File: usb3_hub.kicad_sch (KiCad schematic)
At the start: 63 parts, among them Q2601 QS6M4, U2601 UPD720210K8-BAF-A, Y2601 24MHz

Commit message: Fix schematic ERC errors
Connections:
- net U34.D+: no longer names the net of U2601.35 (U2DP4)
- net U34.D-: no longer names the net of U2601.36 (U2DN4)
- net U34.RX+: no longer names the net of U2601.32 (U3RXDP4)
- net U34.RX-: no longer names the net of U2601.33 (U3RXDN4)
- net U34.TX+: no longer names the net of U2601.29 (U3TXDP4)
- net U34.TX-: no longer names the net of U2601.30 (U3TXDN4)
- no-connect marks 2 -> 8

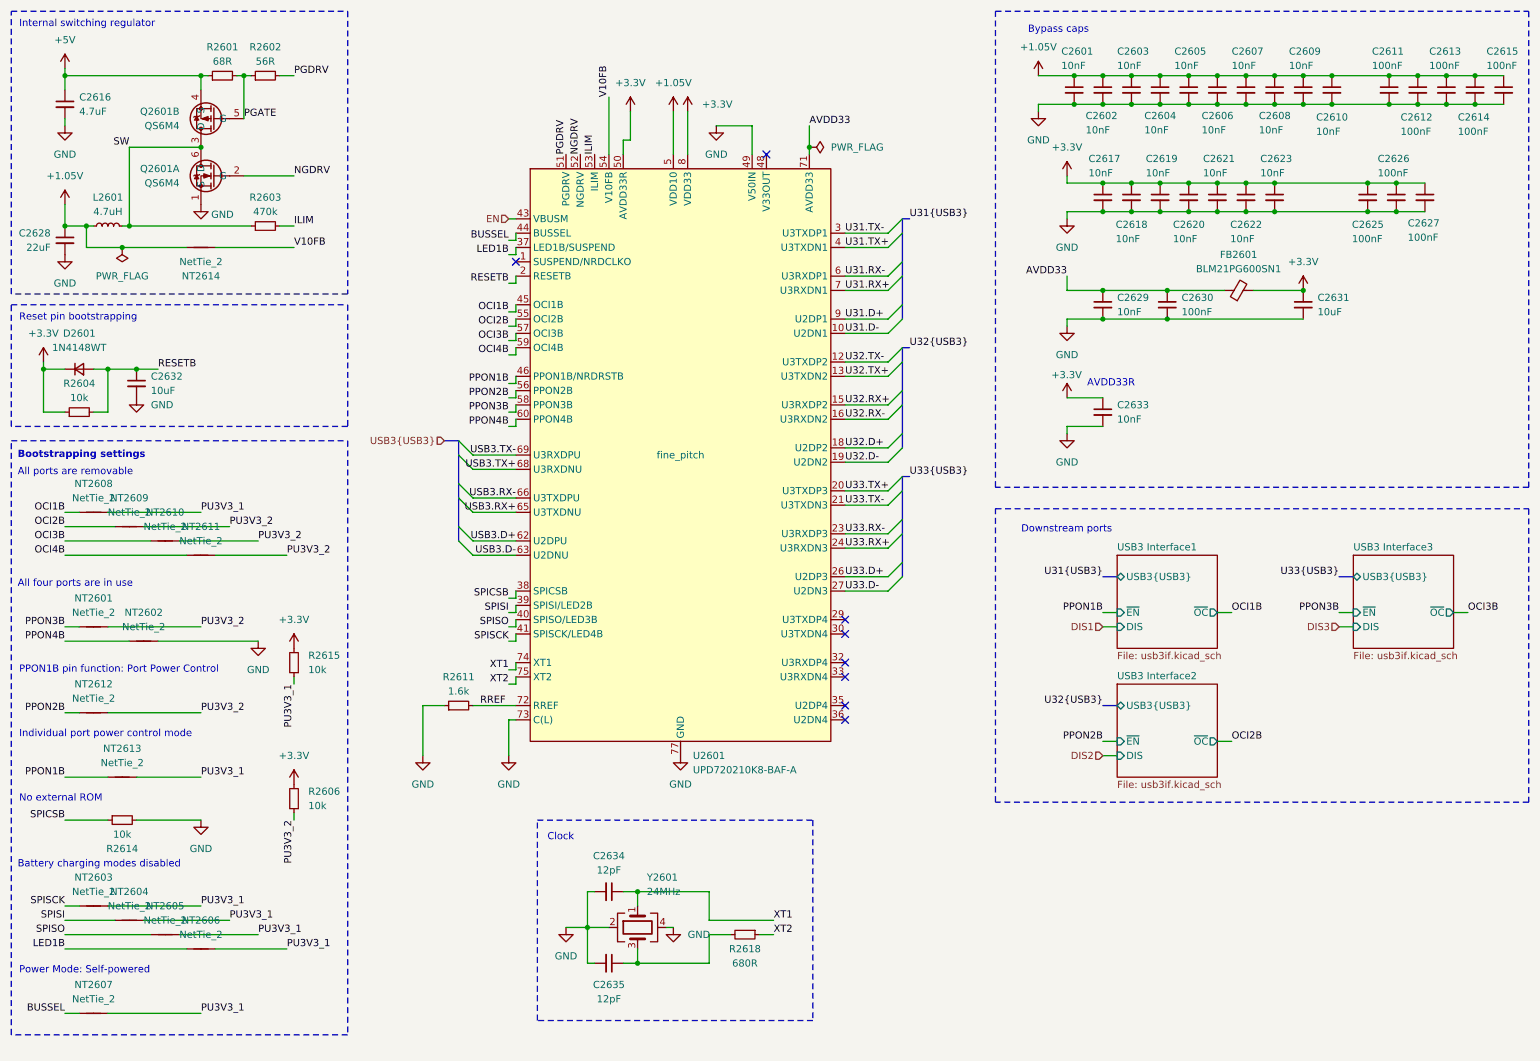
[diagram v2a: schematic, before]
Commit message: Reannotate components
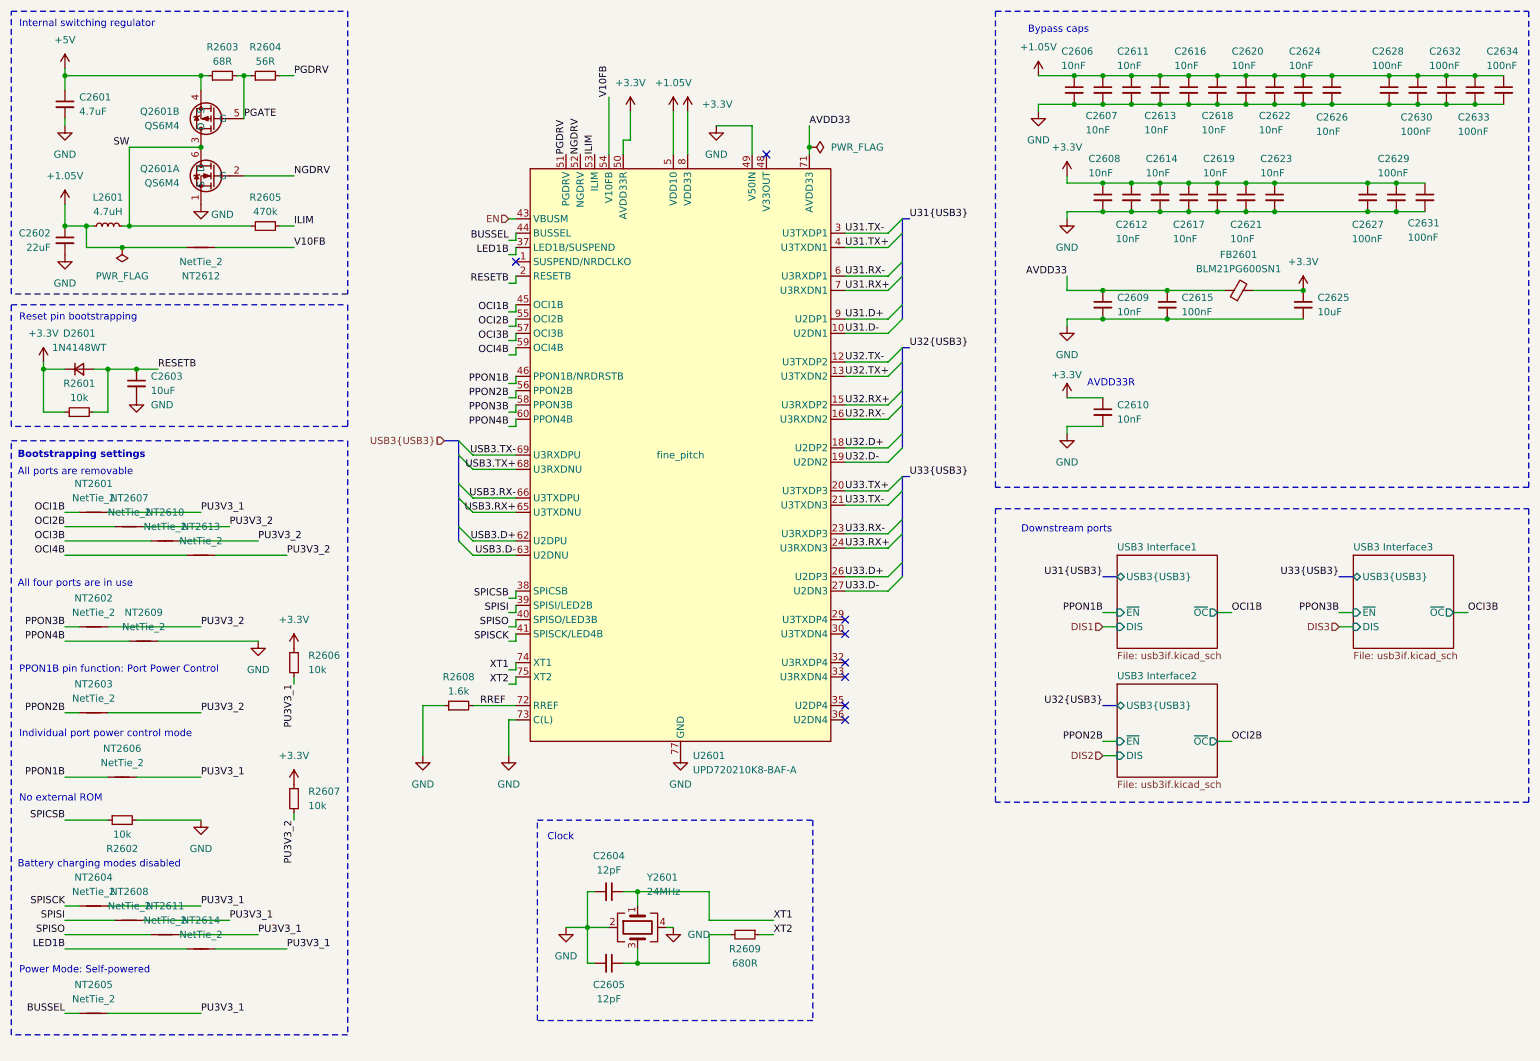
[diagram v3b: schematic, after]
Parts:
- renumbered C2616 to C2601, C2628 to C2602, C2632 to C2603, C2634 to C2604, C2635 to C2605, C2601 to C2606, C2602 to C2607, C2617 to C2608, C2629 to C2609, C2633 to C2610, C2603 to C2611, C2618 to C2612, C2604 to C2613, C2619 to C2614, C2630 to C2615, C2605 to C2616, C2620 to C2617, C2606 to C2618, C2621 to C2619, C2607 to C2620, C2622 to C2621, C2608 to C2622, C2609 to C2624, C2631 to C2625, C2610 to C2626, C2625 to C2627, C2611 to C2628, C2626 to C2629, C2612 to C2630, C2627 to C2631, C2613 to C2632, C2614 to C2633, C2615 to C2634, NT2608 to NT2601, NT2601 to NT2602, NT2612 to NT2603, NT2603 to NT2604, NT2607 to NT2605, NT2613 to NT2606, NT2609 to NT2607, NT2604 to NT2608, NT2602 to NT2609, NT2605 to NT2611, NT2614 to NT2612, NT2611 to NT2613, NT2606 to NT2614, R2604 to R2601, R2614 to R2602, R2601 to R2603, R2602 to R2604, R2603 to R2605, R2615 to R2606, R2606 to R2607, R2611 to R2608, R2618 to R2609

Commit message: Silkscreen mostly done
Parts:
- C2606, C2607, C2608, C2609, C2610, C2611, C2612, C2613, C2614, C2616, C2617, C2618, C2619, C2620, C2621, C2622, C2623, C2624, C2626: value 10nF -> 100nF; LCSC C76941 -> C76934
- C2615, C2627, C2628, C2629, C2630, C2631, C2632, C2633, C2634: value 100nF -> 1uF; LCSC C1525 -> C52923
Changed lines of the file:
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@@
 		(polyline
 			(pts
-				(xy 104.14 134.62) (xy 104.14 114.3) (xy 99.06 114.3) (xy 99.06 134.62)
+				(xy 104.14 88.9) (xy 104.14 52.07) (xy 93.98 52.07) (xy 93.98 88.9)
 			)
 			(stroke
@@
 		(polyline
 			(pts
-				(xy 104.14 88.9) (xy 104.14 52.07) (xy 93.98 52.07) (xy 93.98 88.9)
+				(xy 163.83 49.53) (xy 166.37 49.53) (xy 166.37 140.97) (xy 163.83 140.97)
 			)
 			(stroke
@@
 		(polyline
 			(pts
-				(xy 163.83 49.53) (xy 166.37 49.53) (xy 166.37 140.97) (xy 163.83 140.97)
+				(xy 104.14 134.62) (xy 104.14 114.3) (xy 99.06 114.3) (xy 99.06 134.62)
 			)
 			(stroke
@@
 			)
 		)
-		(property "Value" "10nF"
+		(property "Value" "100nF"
 			(at 210.82 67.3162 0)
 			(effects
@@
 			)
 		)
-		(property "LCSC" "C76941"
+		(property "LCSC" "C76934"
 			(at 208.28 66.04 0)
 			(effects
@@
 			)
 		)
-		(property "Value" "10nF"
+		(property "Value" "100nF"
 			(at 241.3 23.622 0)
 			(effects
@@
 			)
 		)
-		(property "LCSC" "C76941"
+		(property "LCSC" "C76934"
 			(at 243.84 27.94 0)
 			(effects
@@
 			)
 		)
-		(property "Value" "100nF"
+		(property "Value" "1uF"
 			(at 261.112 35.306 0)
 			(effects
@@
 			)
 		)
-		(property "LCSC" "C1525"
+		(property "LCSC" "C52923"
 			(at 264.16 27.94 0)
 			(effects
@@
 			)
 		)
-		(property "Value" "10nF"
+		(property "Value" "100nF"
 			(at 231.14 23.622 0)
 			(effects
@@
 			)
 		)
-		(property "LCSC" "C76941"
+		(property "LCSC" "C76934"
 			(at 233.68 27.94 0)
 			(effects
@@
 			)
 		)
-		(property "Value" "10nF"
+		(property "Value" "100nF"
 			(at 246.126 35.306 0)
 			(effects
@@
 			)
 		)
-		(property "LCSC" "C76941"
+		(property "LCSC" "C76934"
 			(at 248.92 27.94 0)
 			(effects
@@
 			)
 		)
-		(property "Value" "100nF"
+		(property "Value" "1uF"
 			(at 271.272 35.306 0)
 			(effects
@@
 			)
 		)
-		(property "LCSC" "C1525"
+		(property "LCSC" "C52923"
 			(at 274.32 27.94 0)
 			(effects
@@
 			)
 		)
-		(property "Value" "10nF"
+		(property "Value" "100nF"
 			(at 205.74 42.672 0)
 			(effects
@@
 			)
 		)
-		(property "LCSC" "C76941"
+		(property "LCSC" "C76934"
 			(at 208.28 46.99 0)
 			(effects
@@
 			)
 		)
-		(property "Value" "100nF"
+		(property "Value" "1uF"
 			(at 256.032 23.622 0)
 			(effects
@@
 			)
 		)
-		(property "LCSC" "C1525"
+		(property "LCSC" "C52923"
 			(at 259.08 27.94 0)
 			(effects
@@
 			)
 		)
-		(property "Datasheet" ""
+		(property "Datasheet" "https://www.lcsc.com/datasheet/lcsc_datasheet_2410121931_RENESAS-UPD720210K8-BAF-A_C2982859.pdf"
 			(at 133.35 92.71 0)
 			(effects
@@
 					(size 1.27 1.27)
 				)
+				(hide yes)
 			)
 		)
@@
 			)
 		)
-		(property "Value" "100nF"
+		(property "Value" "1uF"
 			(at 222.25 67.3162 0)
 			(effects
@@
 			)
 		)
-		(property "LCSC" "C1525"
+		(property "LCSC" "C52923"
 			(at 219.71 66.04 0)
 			(effects
@@
 			)
 		)
-		(property "Value" "10nF"
+		(property "Value" "100nF"
 			(at 220.98 23.622 0)
 			(effects
@@
 			)
 		)
-		(property "LCSC" "C76941"
+		(property "LCSC" "C76934"
 			(at 223.52 27.94 0)
 			(effects
@@
 			)
 		)
-		(property "Value" "100nF"
+		(property "Value" "1uF"
 			(at 257.048 42.672 0)
 			(effects
@@
 			)
 		)
-		(property "LCSC" "C1525"
+		(property "LCSC" "C52923"
 			(at 260.35 46.99 0)
 			(effects
@@
 			)
 		)
-		(property "Value" "10nF"
+		(property "Value" "100nF"
 			(at 210.82 23.622 0)
 			(effects
@@
 			)
 		)
-		(property "LCSC" "C76941"
+		(property "LCSC" "C76934"
 			(at 213.36 27.94 0)
 			(effects
@@
 			)
 		)
-		(property "Value" "10nF"
+		(property "Value" "100nF"
 			(at 210.82 86.3662 0)
 			(effects
@@
 			)
 		)
-		(property "LCSC" "C76941"
+		(property "LCSC" "C76934"
 			(at 208.28 85.09 0)
 			(effects
@@
 			)
 		)
-		(property "Value" "100nF"
+		(property "Value" "1uF"
 			(at 266.192 23.622 0)
 			(effects
@@
 			)
 		)
-		(property "LCSC" "C1525"
+		(property "LCSC" "C52923"
 			(at 269.24 27.94 0)
 			(effects
@@
 			)
 		)
-		(property "Value" "10nF"
+		(property "Value" "100nF"
 			(at 236.22 42.672 0)
 			(effects
@@
 			)
 		)
-		(property "LCSC" "C76941"
+		(property "LCSC" "C76934"
 			(at 238.76 46.99 0)
 			(effects
@@
 			)
 		)
-		(property "Value" "10nF"
+		(property "Value" "100nF"
 			(at 235.966 35.052 0)
 			(effects
@@
 			)
 		)
-		(property "LCSC" "C76941"
+		(property "LCSC" "C76934"
 			(at 238.76 27.94 0)
 			(effects
@@
 			)
 		)
-		(property "Value" "100nF"
+		(property "Value" "1uF"
 			(at 252.476 54.356 0)
 			(effects
@@
 			)
 		)
-		(property "LCSC" "C1525"
+		(property "LCSC" "C52923"
 			(at 255.27 46.99 0)
 			(effects
@@
 			)
 		)
-		(property "Value" "10nF"
+		(property "Value" "100nF"
 			(at 220.726 54.356 0)
 			(effects
@@
 			)
 		)
-		(property "LCSC" "C76941"
+		(property "LCSC" "C76934"
 			(at 223.52 46.99 0)
 			(effects
@@
 			)
 		)
-		(property "Value" "10nF"
+		(property "Value" "100nF"
 			(at 230.886 54.356 0)
 			(effects
@@
 			)
 		)
-		(property "LCSC" "C76941"
+		(property "LCSC" "C76934"
 			(at 233.68 46.99 0)
 			(effects
@@
 			)
 		)
-		(property "Value" "10nF"
+		(property "Value" "100nF"
 			(at 205.232 35.052 0)
 			(effects
@@
 			)
 		)
-		(property "LCSC" "C76941"
+		(property "LCSC" "C76934"
 			(at 208.28 27.94 0)
 			(effects
@@
 			)
 		)
-		(property "Value" "100nF"
+		(property "Value" "1uF"
 			(at 276.352 23.622 0)
 			(effects
@@
 			)
 		)
-		(property "LCSC" "C1525"
+		(property "LCSC" "C52923"
 			(at 279.4 27.94 0)
 			(effects
@@
 			)
 		)
-		(property "Value" "100nF"
+		(property "Value" "1uF"
 			(at 262.382 54.102 0)
 			(effects
@@
 			)
 		)
-		(property "LCSC" "C1525"
+		(property "LCSC" "C52923"
 			(at 265.43 46.99 0)
 			(effects
@@
 			)
 		)
-		(property "Value" "10nF"
+		(property "Value" "100nF"
 			(at 200.914 23.622 0)
 			(effects
@@
 			)
 		)
-		(property "LCSC" "C76941"
+		(property "LCSC" "C76934"
 			(at 203.2 27.94 0)
 			(effects
@@
 			)
 		)
-		(property "Value" "10nF"
+		(property "Value" "100nF"
 			(at 210.566 54.356 0)
 			(effects
@@
 			)
 		)
-		(property "LCSC" "C76941"
+		(property "LCSC" "C76934"
 			(at 213.36 46.99 0)
 			(effects
@@
 			)
 		)
-		(property "Value" "10nF"
+		(property "Value" "100nF"
 			(at 215.646 35.052 0)
 			(effects
@@
 			)
 		)
-		(property "LCSC" "C76941"
+		(property "LCSC" "C76934"
 			(at 218.44 27.94 0)
 			(effects
@@
 			)
 		)
-		(property "Value" "10nF"
+		(property "Value" "100nF"
 			(at 226.06 42.672 0)
 			(effects
@@
 			)
 		)
-		(property "LCSC" "C76941"
+		(property "LCSC" "C76934"
 			(at 228.6 46.99 0)
 			(effects
@@
 			)
 		)
-		(property "Value" "10nF"
+		(property "Value" "100nF"
 			(at 215.9 42.672 0)
 			(effects
@@
 			)
 		)
-		(property "LCSC" "C76941"
+		(property "LCSC" "C76934"
 			(at 218.44 46.99 0)
 			(effects
@@
 			)
 		)
-		(property "Value" "10nF"
+		(property "Value" "100nF"
 			(at 225.806 35.052 0)
 			(effects
@@
 			)
 		)
-		(property "LCSC" "C76941"
+		(property "LCSC" "C76934"
 			(at 228.6 27.94 0)
 			(effects

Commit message: Finish the board redesign with SoM on the bottom
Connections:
- net USB3.RX+: now also U2601.66 (U3TXDPU); no longer U2601.65 (U3TXDNU)
- net USB3.RX-: now also U2601.65 (U3TXDNU); no longer U2601.66 (U3TXDPU)
- net USB3.TX+: now also U2601.69 (U3RXDPU); no longer U2601.68 (U3RXDNU)
- net USB3.TX-: now also U2601.68 (U3RXDNU); no longer U2601.69 (U3RXDPU)
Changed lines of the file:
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@@
 	)
 	(label "USB3.TX-"
-		(at 104.14 92.71 180)
+		(at 104.14 95.25 180)
 		(effects
 			(font
@@
 	)
 	(label "USB3.RX+"
-		(at 104.14 102.87 180)
+		(at 104.14 100.33 180)
 		(effects
 			(font
@@
 	)
 	(label "USB3.TX+"
-		(at 104.14 95.25 180)
+		(at 104.14 92.71 180)
 		(effects
 			(font
@@
 	)
 	(label "USB3.RX-"
-		(at 104.14 100.33 180)
+		(at 104.14 102.87 180)
 		(effects
 			(font
@@
 		(polyline
 			(pts
-				(xy 104.14 88.9) (xy 104.14 52.07) (xy 93.98 52.07) (xy 93.98 88.9)
+				(xy 163.83 49.53) (xy 166.37 49.53) (xy 166.37 140.97) (xy 163.83 140.97)
 			)
 			(stroke
@@
 		(polyline
 			(pts
-				(xy 163.83 49.53) (xy 166.37 49.53) (xy 166.37 140.97) (xy 163.83 140.97)
+				(xy 104.14 88.9) (xy 104.14 52.07) (xy 93.98 52.07) (xy 93.98 88.9)
 			)
 			(stroke
@@
 			)
 		)
-		(property "Description" ""
+		(property "Description" "Unpolarized capacitor, small symbol"
 			(at 120.65 170.18 0)
 			(effects
@@
 			)
 		)
-		(property "Datasheet" ""
+		(property "Datasheet" "~"
 			(at 125.73 176.53 0)
 			(effects
@@
 			)
 		)
-		(property "Description" ""
+		(property "Description" "Four pin crystal, GND on pins 2 and 4"
 			(at 125.73 176.53 0)
 			(effects
@@
 			)
 		)
-		(property "Description" ""
+		(property "Description" "Unpolarized capacitor, small symbol"
 			(at 120.65 182.88 0)
 			(effects

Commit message: Further refinements
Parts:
- removed NT2601, NT2602, NT2603, NT2604, NT2605, NT2606, NT2607, NT2608, NT2609, NT2610, NT2611, NT2613, NT2614: NetTie_2, Hatlabs:NetTie-2_SMD_Pad0.2mm, symbol Device:NetTie_2
- removed R2606, R2607: 10k, Resistor_SMD:R_0402_1005Metric, symbol Device:R_Small
- added R2610, R2611, R2612, R2613, R2614, R2615, R2616, R2617, R2618, R2619, R2620, R2621, R2622: 10k, Resistor_SMD:R_0402_1005Metric, symbol Device:R_Small
- added TP1208: TestPoint, TestPoint:TestPoint_Pad_D1.0mm, symbol Connector:TestPoint
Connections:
- net +1.05V: now also TP1208.1
- net +3.3V: now also R2610.1, R2611.1, R2612.1, R2613.1, R2614.1, R2616.1, R2617.1, R2618.2, R2619.2, R2620.2, R2621.2, R2622.2
- net BUSSEL: now also R2622.1
- net GND: now also R2615.1
- net LED1B: now also R2621.1
- net OCI1B: now also R2610.2
- net OCI2B: now also R2611.2
- net OCI3B: now also R2612.2
- net OCI4B: now also R2613.2
- net PPON1B: now also R2616.2
- net PPON2B: now also R2617.2
- net PPON3B: now also R2614.2
- net PPON4B: now also R2615.2
- net SPISCK: now also R2618.1
- net SPISI: now also R2619.1
- net SPISO: now also R2620.1
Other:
- note added: "Three ports are in use"
- note removed: "All four ports are in use"
